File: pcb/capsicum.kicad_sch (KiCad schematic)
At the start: 52 parts, among them J1 USB4510-03-1-A_REVA, J2 Screw_Terminal_01x02, Q1 BSS83P, Q2 BC817-16LT3G, SW1 SW_SPDT, SW2 SW_Push_Dual, SW3 SW_SPDT, SW4 SW_Push_Dual, U1 ESP32-C3-WROOM-02, U3 AP2112K, U4 MCP73831-2-OT

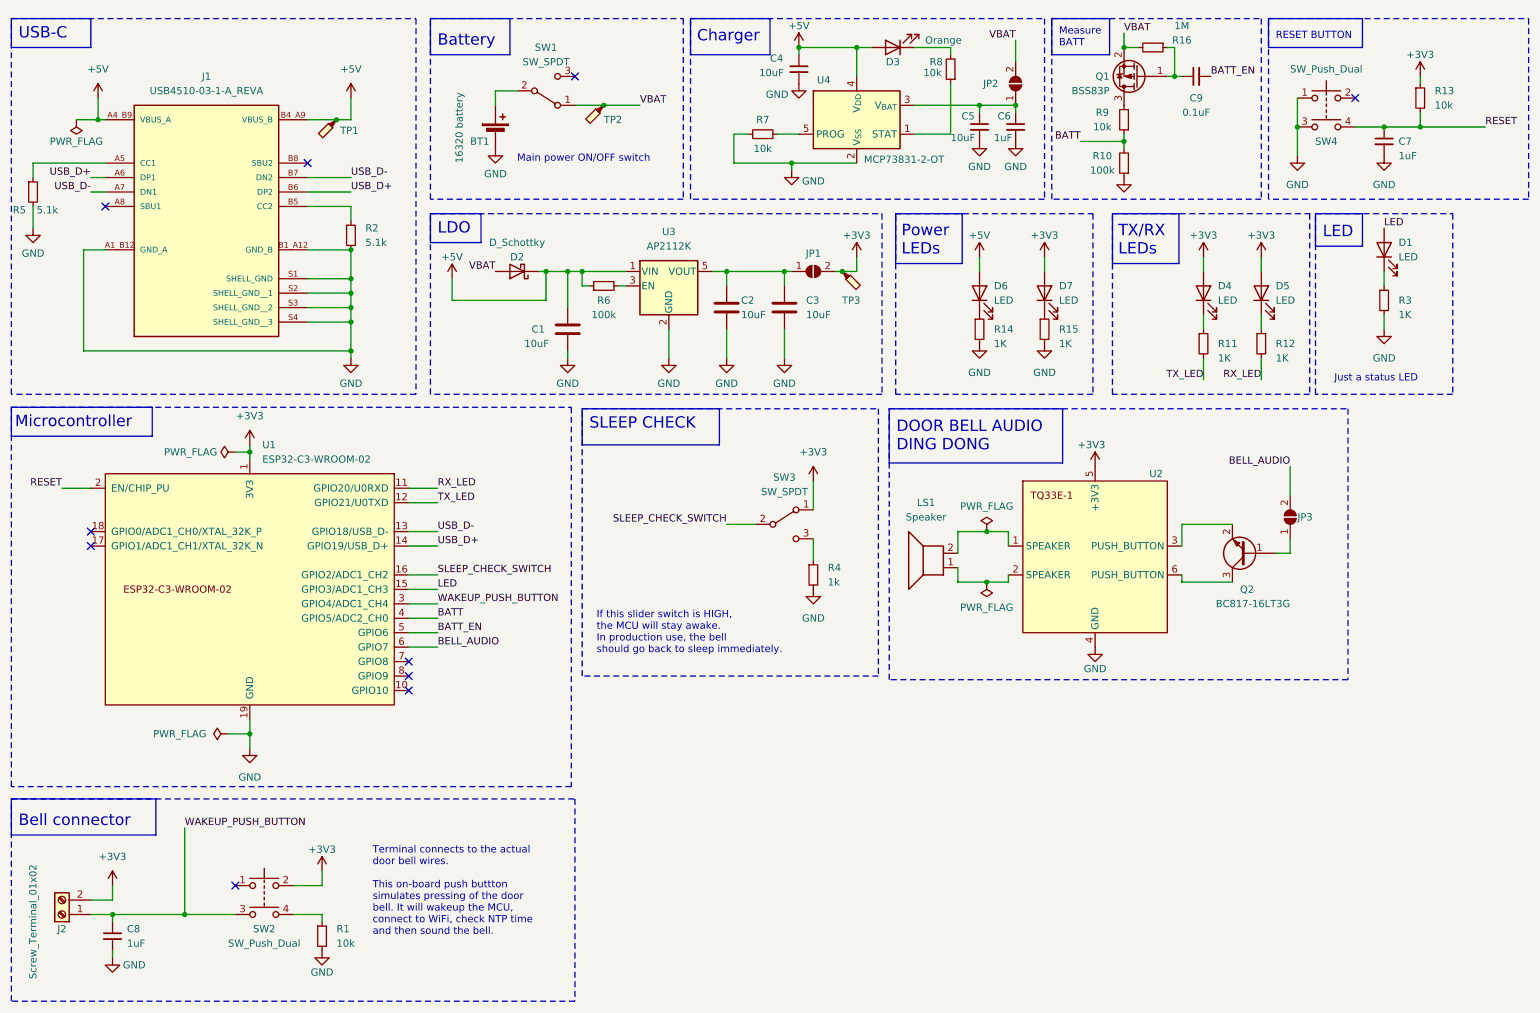
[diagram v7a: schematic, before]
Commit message: feat: associate push buttons and slide switches to MPN and footprints
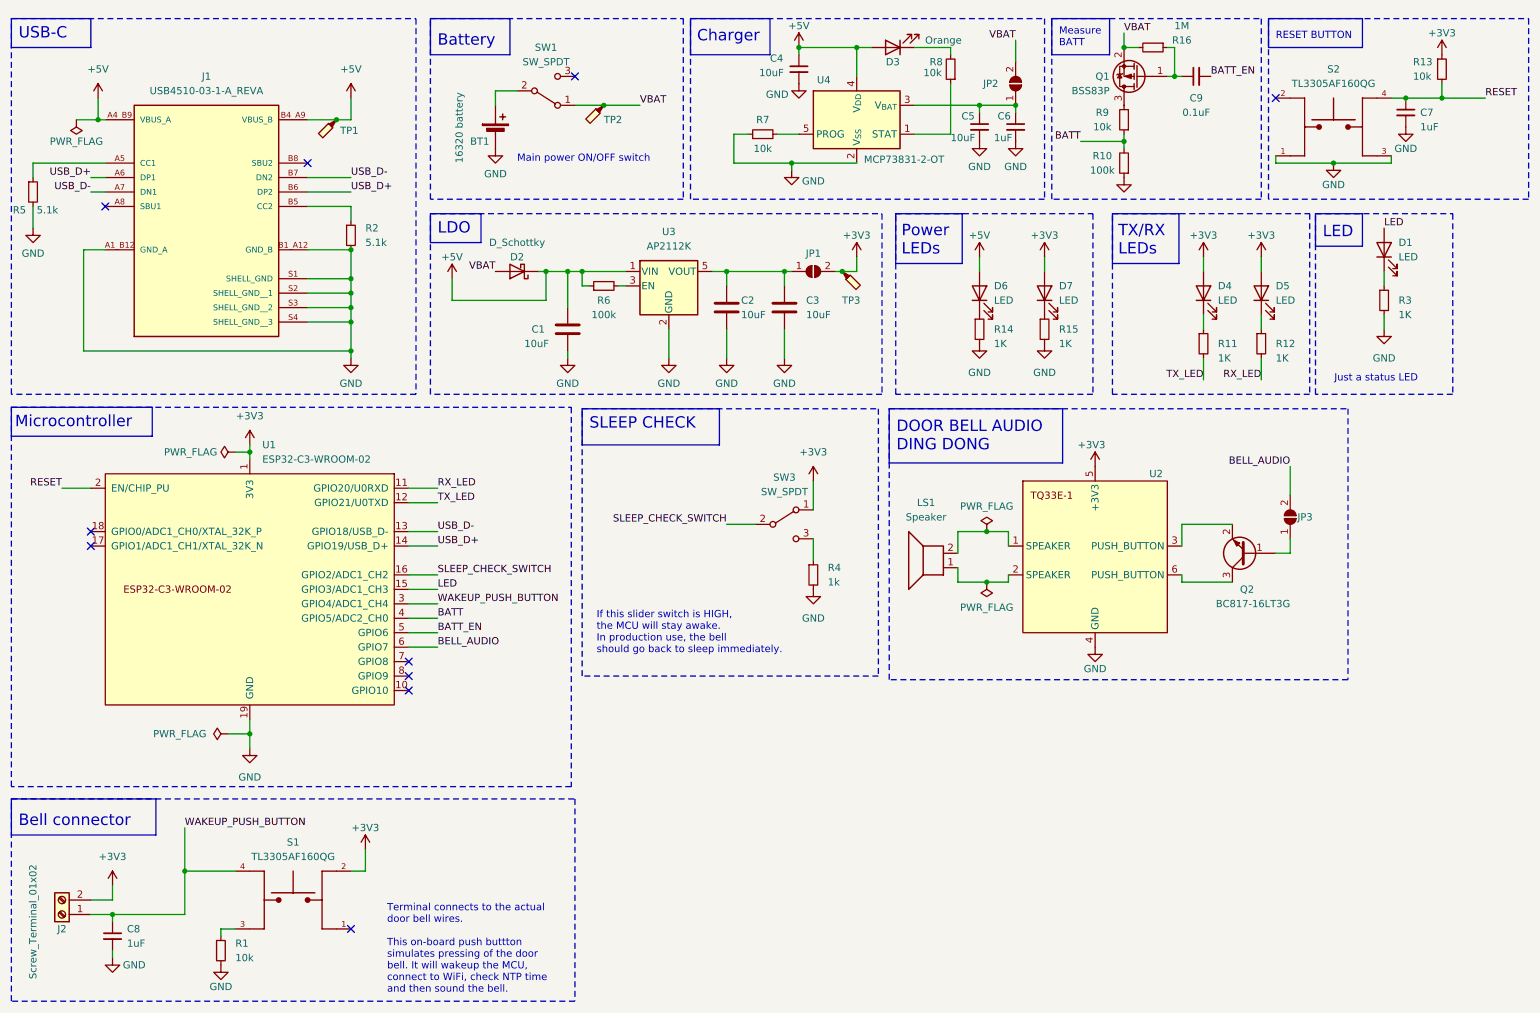
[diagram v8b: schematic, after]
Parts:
- removed SW2, SW4: SW_Push_Dual, symbol Switch:SW_Push_Dual
- added S1, S2: TL3305AF160QG, Push button:SW_TL3305AF160QG, symbol Push button:TL3305AF160QG
- SW1: footprint (none) -> Button_Switch_SMD:SW_SPDT_PCM12; Link (none) -> https://www.pcbway.com/components/detail/CUS12TB/705754/; MPN (none) -> CUS-12TB; Package (none) -> SMD; Vendor (none) -> PCBWay
- SW3: footprint (none) -> Button_Switch_SMD:SW_SPDT_PCM12; Link (none) -> https://www.pcbway.com/components/detail/CUS12TB/705754/; MPN (none) -> CUS-12TB; Package (none) -> SMD
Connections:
- net +3V3: now also S1.2
- net GND: now also S2.1, S2.3
- net RESET: now also S2.4
- net WAKEUP_PUSH_BUTTON: now also S1.4
- net at R1.1: now also S1.3
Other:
- moved on the sheet: C7, R1, R13
